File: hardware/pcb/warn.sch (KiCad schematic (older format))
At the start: 16 parts, among them CON2 MMCX_CONN, Q1 Q_NPN_BEC, U8 TPS61041, U9 ZXMHC6A07N8

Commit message: pre major restructuring commit
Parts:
- removed Q1: Q_NPN_BEC, Housings_SOT-23_SOT-143_TSOT-6:SOT-23, symbol Q_NPN_BEC-RESCUE-aero
- removed R15, R16: 3k, Resistors_SMD:R_0603, symbol R
- removed U9: ZXMHC6A07N8, Power_Integrations:SO-8, symbol ZXMHC6A07N8
- added Q1: BSS138, Housings_SOT-23_SOT-143_TSOT-6:SOT-23, symbol BSS138
- added R14: 30k, Resistors_SMD:R_0402, symbol R
- added U10, U11: BU4SU69G2, aero:SSOP-5, symbol BU4SU69G2
- added U12: NC7WZ17, Housings_SOT-23_SOT-143_TSOT-6:SC-70-6, symbol NC7WZ17
- C29: renamed from C32; footprint Capacitors_SMD:C_0603 -> Capacitors_SMD:C_0402
- C30: renamed from C33; footprint Capacitors_SMD:C_0603 -> Capacitors_SMD:C_0402
- C31: renamed from C34; footprint Capacitors_SMD:C_0603 -> Capacitors_SMD:C_0402
- L1: renamed from L4; footprint aero:SDR0703 -> aero:IND-744029100
- R11: renamed from R12; value 120 -> 200; footprint Resistors_SMD:R_0603 -> Resistors_SMD:R_0402
- R12: renamed from R13; footprint Resistors_SMD:R_0603 -> Resistors_SMD:R_0402
- R13: renamed from R14; value 140k -> 309k; footprint Resistors_SMD:R_0603 -> Resistors_SMD:R_0402
- renumbered D2 to D1, D3 to D2, U8 to U9
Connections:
- net labels added: +10V
- net labels removed: +24V
- wire segments 52 -> 38
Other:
- note removed: "Add a flyback diode?"
- note removed: "Confirm pin assignments of NPN"
- note removed: "NOTE: Update R when LED is picked out"
- note removed: "Using VBATT here is probably a bad idea"
- moved on the sheet: AUD1, C29, C30, C31, CON2, D2, L1, R12, R13, U9

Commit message: more progress on new layout
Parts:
- renumbered C29 to C27, C30 to C28, C31 to C29, R11 to R10, R12 to R11, R13 to R12, R14 to R13
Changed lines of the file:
@@
 $EndComp
 $Comp
-L C C29
+L C C27
 U 1 1 55381689
 P 1650 5475
-F 0 "C29" H 1675 5575 50  0000 L CNN
+F 0 "C27" H 1675 5575 50  0000 L CNN
 F 1 "4.7uF" H 1675 5375 50  0000 L CNN
 F 2 "Capacitors_SMD:C_0402" H 1688 5325 30  0001 C CNN
@@
 $EndComp
 $Comp
-L R R12
+L R R11
 U 1 1 55381851
 P 4200 5025
-F 0 "R12" V 4280 5025 50  0000 C CNN
+F 0 "R11" V 4280 5025 50  0000 C CNN
 F 1 "2.21m" V 4200 5025 50  0000 C CNN
 F 2 "Resistors_SMD:R_0402" V 4130 5025 30  0001 C CNN
@@
 $EndComp
 $Comp
-L R R13
+L R R12
 U 1 1 5538187A
 P 4200 5625
-F 0 "R13" V 4280 5625 50  0000 C CNN
+F 0 "R12" V 4280 5625 50  0000 C CNN
 F 1 "309k" V 4200 5625 50  0000 C CNN
 F 2 "Resistors_SMD:R_0402" V 4130 5625 30  0001 C CNN
@@
 $EndComp
 $Comp
-L C C30
+L C C28
 U 1 1 553818B9
 P 4600 5025
-F 0 "C30" H 4625 5125 50  0000 L CNN
+F 0 "C28" H 4625 5125 50  0000 L CNN
 F 1 "22pF" H 4625 4925 50  0000 L CNN
 F 2 "Capacitors_SMD:C_0402" H 4638 4875 30  0001 C CNN
@@
 $EndComp
 $Comp
-L C C31
+L C C29
 U 1 1 553818E7
 P 4950 5025
-F 0 "C31" H 4975 5125 50  0000 L CNN
+F 0 "C29" H 4975 5125 50  0000 L CNN
 F 1 "100nF" H 4975 4925 50  0000 L CNN
 F 2 "Capacitors_SMD:C_0402" H 4988 4875 30  0001 C CNN
@@
 $EndComp
 $Comp
-L R R11
+L R R10
 U 1 1 55381B8F
 P 2850 2800
-F 0 "R11" V 2930 2800 50  0000 C CNN
+F 0 "R10" V 2930 2800 50  0000 C CNN
 F 1 "200" V 2850 2800 50  0000 C CNN
 F 2 "Resistors_SMD:R_0402" V 2780 2800 30  0001 C CNN
@@
 $EndComp
 $Comp
-L R R14
+L R R13
 U 1 1 55B1064F
 P 6175 5000
-F 0 "R14" V 6255 5000 50  0000 C CNN
+F 0 "R13" V 6255 5000 50  0000 C CNN
 F 1 "30k" V 6175 5000 50  0000 C CNN
 F 2 "Resistors_SMD:R_0402" V 6105 5000 30  0001 C CNN

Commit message: pre-net import
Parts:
- added U14: NC7WZ17, Housings_SOT-23_SOT-143_TSOT-6:SC-70-6, symbol NC7WZ17
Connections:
- net +3V: now also U14.5 (+3V), U14.5 (+3V)
- net GND: now also U14.2 (GND), U14.2 (GND)
- net WARN_LED_A: now also U12.1
- net WARN_LED_B: now also U14.1, U14.3; no longer U12.1
- net at CON2.1 (SIG), U12.4: now also U12.6
- net at CON2.2 (GND), CON2.3 (GND), CON2.4 (GND)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: now also U14.4, U14.6; no longer U12.6
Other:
- moved on the sheet: U12A, U12B
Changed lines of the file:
@@
 Text HLabel 5675 5650 0    60   Input ~ 0
 PIEZO_OUT
-Text HLabel 7975 2575 0    60   Input ~ 0
+Text HLabel 7950 2575 0    60   Input ~ 0
 WARN_LED_A
-Text HLabel 7975 3100 0    60   Input ~ 0
+Text HLabel 7950 3500 0    60   Input ~ 0
 WARN_LED_B
 Text HLabel 1700 2800 0    60   Input ~ 0
@@
 EN needs to be at least\n1.2v
 $Comp
-L MMCX_CONN CON2
-U 1 1 5540F4C0
-P 9900 2675
-F 0 "CON2" H 10100 2875 60  0000 C CNN
-F 1 "MMCX_CONN" H 10050 2525 60  0000 C CNN
-F 2 "aero:CONMMCX002-SMD" H 9900 2675 60  0001 C CNN
-F 3 "" H 9900 2675 60  0000 C CNN
-	1    9900 2675
-	1    0    0    -1
-$EndComp
-$Comp
 L PIEZO AUD1
 U 1 1 554BE33E
@@
 L NC7WZ17 U12
 U 1 1 55B160CF
-P 8425 3100
-F 0 "U12" H 8525 3225 60  0000 C CNN
-F 1 "NC7WZ17" H 8600 2925 60  0001 C CNN
-F 2 "Housings_SOT-23_SOT-143_TSOT-6:SC-70-6" H 8425 3100 60  0001 C CNN
-F 3 "" H 8425 3100 60  0000 C CNN
-	1    8425 3100
+P 8475 2575
+F 0 "U12" H 8575 2700 60  0000 C CNN
+F 1 "NC7WZ17" H 8650 2400 60  0001 C CNN
+F 2 "Housings_SOT-23_SOT-143_TSOT-6:SC-70-6" H 8475 2575 60  0001 C CNN
+F 3 "" H 8475 2575 60  0000 C CNN
+	1    8475 2575
 	1    0    0    -1
 $EndComp
@@
 L NC7WZ17 U12
 U 2 1 55B161A1
-P 8450 2575
-F 0 "U12" H 8550 2700 60  0000 C CNN
-F 1 "NC7WZ17" H 8625 2400 60  0001 C CNN
-F 2 "Housings_SOT-23_SOT-143_TSOT-6:SC-70-6" H 8450 2575 60  0001 C CNN
-F 3 "" H 8450 2575 60  0000 C CNN
-	2    8450 2575
+P 8450 2925
+F 0 "U12" H 8550 3050 60  0000 C CNN
+F 1 "NC7WZ17" H 8625 2750 60  0001 C CNN
+F 2 "Housings_SOT-23_SOT-143_TSOT-6:SC-70-6" H 8450 2925 60  0001 C CNN
+F 3 "" H 8450 2925 60  0000 C CNN
+	2    8450 2925
 	1    0    0    -1
 $EndComp
@@
 Wire Wire Line
 	2350 2800 2700 2800
-Wire Wire Line
-	10675 2575 10675 3100
 Connection ~ 10675 2650
 Connection ~ 10675 2725
@@
 	5675 5650 5875 5650
 Wire Wire Line
-	8150 3100 7975 3100
-Wire Wire Line
-	7975 2575 8175 2575
-Wire Wire Line
-	8750 2575 9650 2575
-Wire Wire Line
-	10675 3100 8725 3100
-Wire Wire Line
 	3900 4725 6225 4725
+$Comp
+L NC7WZ17 U14
+U 1 1 561D6D8E
+P 8425 3500
+F 0 "U14" H 8525 3625 60  0000 C CNN
+F 1 "NC7WZ17" H 8600 3325 60  0001 C CNN
+F 2 "Housings_SOT-23_SOT-143_TSOT-6:SC-70-6" H 8425 3500 60  0001 C CNN
+F 3 "" H 8425 3500 60  0000 C CNN
+	1    8425 3500
+	1    0    0    -1
+$EndComp
+$Comp
+L NC7WZ17 U14
+U 2 1 561D6E0B
+P 8450 3925
+F 0 "U14" H 8550 4050 60  0000 C CNN
+F 1 "NC7WZ17" H 8625 3750 60  0001 C CNN
+F 2 "Housings_SOT-23_SOT-143_TSOT-6:SC-70-6" H 8450 3925 60  0001 C CNN
+F 3 "" H 8450 3925 60  0000 C CNN
+	2    8450 3925
+	1    0    0    -1
+$EndComp
+$Comp
+L MMCX_CONN CON2
+U 1 1 5540F4C0
+P 9900 2675
+F 0 "CON2" H 10100 2875 60  0000 C CNN
+F 1 "MMCX_CONN" H 10050 2525 60  0000 C CNN
+F 2 "aero:CONMMCX002-SMD" H 9900 2675 60  0001 C CNN
+F 3 "" H 9900 2675 60  0000 C CNN
+	1    9900 2675
+	1    0    0    -1
+$EndComp
+Wire Wire Line
+	7950 2575 8200 2575
+Wire Wire Line
+	8175 2925 8050 2925
+Wire Wire Line
+	8050 2925 8050 2575
+Connection ~ 8050 2575
+Wire Wire Line
+	8775 2575 9650 2575
+Wire Wire Line
+	8750 2925 9050 2925
+Wire Wire Line
+	9050 2925 9050 2575
+Connection ~ 9050 2575
+Wire Wire Line
+	7950 3500 8150 3500
+Wire Wire Line
+	8050 3500 8050 3925
+Wire Wire Line
+	8050 3925 8175 3925
+Connection ~ 8050 3500
+Wire Wire Line
+	10675 3500 8725 3500
+Wire Wire Line
+	10675 2575 10675 3500
+Wire Wire Line
+	8750 3925 9050 3925
+Wire Wire Line
+	9050 3925 9050 3500
+Connection ~ 9050 3500
 $EndSCHEMATC

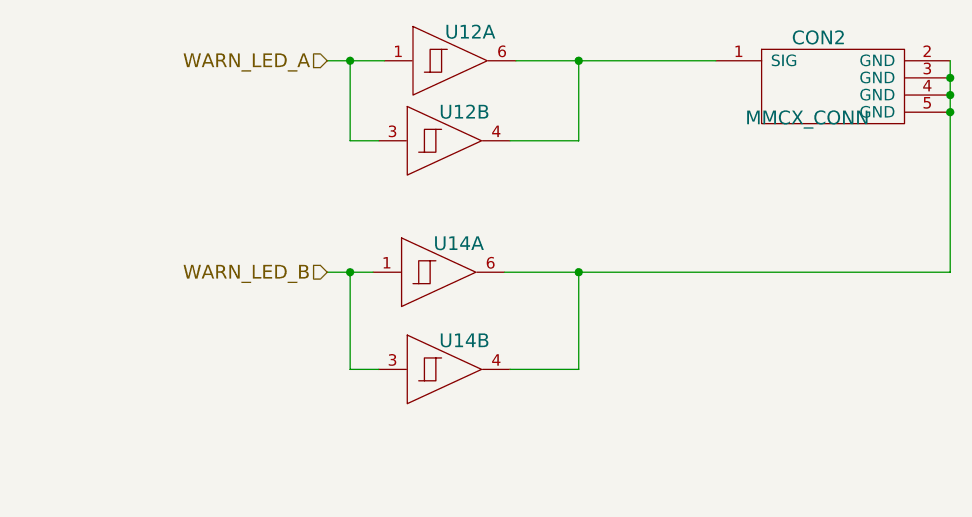
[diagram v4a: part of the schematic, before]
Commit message: passes DRC with stitching
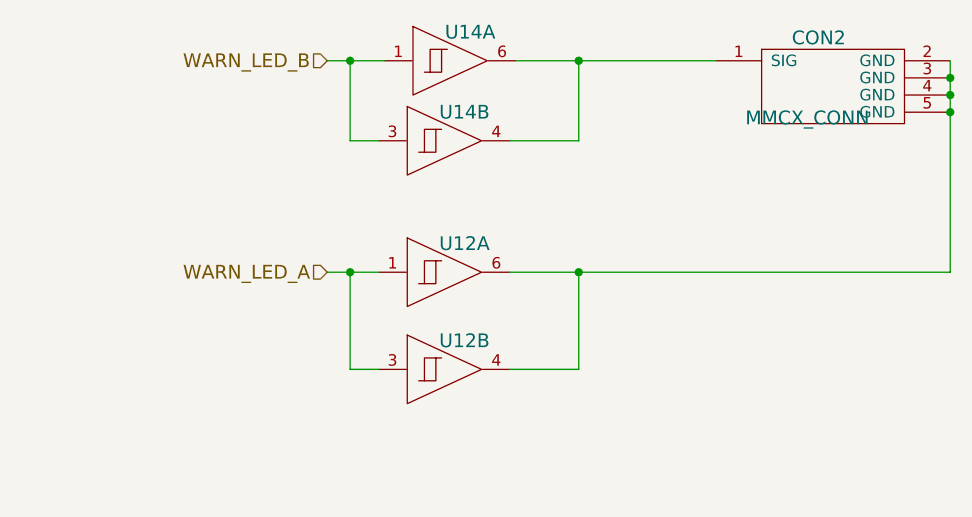
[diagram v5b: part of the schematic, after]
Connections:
- net at U12.4, U12.6: now also CON2.2 (GND), CON2.3 (GND), CON2.4 (GND), CON2.5 (GND); no longer CON2.1 (SIG)
- new net: CON2.1 (SIG), U14.4, U14.6
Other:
- moved on the sheet: U12A, U12B, U14A, U14B
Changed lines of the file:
@@
 Text HLabel 5675 5650 0    60   Input ~ 0
 PIEZO_OUT
+Text HLabel 7950 3500 0    60   Input ~ 0
+WARN_LED_A
 Text HLabel 7950 2575 0    60   Input ~ 0
-WARN_LED_A
-Text HLabel 7950 3500 0    60   Input ~ 0
 WARN_LED_B
 Text HLabel 1700 2800 0    60   Input ~ 0
@@
 L NC7WZ17 U12
 U 1 1 55B160CF
-P 8475 2575
-F 0 "U12" H 8575 2700 60  0000 C CNN
-F 1 "NC7WZ17" H 8650 2400 60  0001 C CNN
-F 2 "Housings_SOT-23_SOT-143_TSOT-6:SC-70-6" H 8475 2575 60  0001 C CNN
-F 3 "" H 8475 2575 60  0000 C CNN
-	1    8475 2575
+P 8450 3500
+F 0 "U12" H 8550 3625 60  0000 C CNN
+F 1 "NC7WZ17" H 8625 3325 60  0001 C CNN
+F 2 "Housings_SOT-23_SOT-143_TSOT-6:SC-70-6" H 8450 3500 60  0001 C CNN
+F 3 "" H 8450 3500 60  0000 C CNN
+	1    8450 3500
 	1    0    0    -1
 $EndComp
@@
 L NC7WZ17 U12
 U 2 1 55B161A1
-P 8450 2925
-F 0 "U12" H 8550 3050 60  0000 C CNN
-F 1 "NC7WZ17" H 8625 2750 60  0001 C CNN
-F 2 "Housings_SOT-23_SOT-143_TSOT-6:SC-70-6" H 8450 2925 60  0001 C CNN
-F 3 "" H 8450 2925 60  0000 C CNN
-	2    8450 2925
+P 8450 3925
+F 0 "U12" H 8550 4050 60  0000 C CNN
+F 1 "NC7WZ17" H 8625 3750 60  0001 C CNN
+F 2 "Housings_SOT-23_SOT-143_TSOT-6:SC-70-6" H 8450 3925 60  0001 C CNN
+F 3 "" H 8450 3925 60  0000 C CNN
+	2    8450 3925
 	1    0    0    -1
 $EndComp
@@
 	0    1    1    0
 $EndComp
-Wire Wire Line
-	2450 5475 2750 5475
-Wire Wire Line
-	1150 5075 1150 5275
-Wire Wire Line
-	1150 5275 2750 5275
-Wire Wire Line
-	1650 5325 1650 5275
-Connection ~ 1650 5275
-Wire Wire Line
-	1650 5625 1650 6025
-Wire Wire Line
-	2400 4725 2200 4725
-Wire Wire Line
-	2200 4725 2200 5275
-Connection ~ 2200 5275
-Wire Wire Line
-	3000 4725 3600 4725
-Wire Wire Line
-	3300 4975 3300 4725
-Connection ~ 3300 4725
-Wire Wire Line
-	4200 5175 4200 5475
-Wire Wire Line
-	3750 5375 4600 5375
-Connection ~ 4200 5375
-Wire Wire Line
-	1650 5975 6175 5975
-Wire Wire Line
-	3300 5975 3300 5825
-Connection ~ 1650 5975
-Wire Wire Line
-	4200 5975 4200 5775
-Connection ~ 3300 5975
-Wire Wire Line
-	4600 5375 4600 5175
-Wire Wire Line
-	4200 4725 4200 4875
-Wire Wire Line
-	4600 4725 4600 4875
-Connection ~ 4200 4725
-Wire Wire Line
-	4950 4725 4950 4875
-Connection ~ 4600 4725
-Wire Wire Line
-	4950 5175 4950 5975
-Connection ~ 4200 5975
-Connection ~ 4950 4725
-Wire Wire Line
-	3000 2800 3400 2800
-Wire Wire Line
-	3400 2800 3400 3000
-Wire Wire Line
-	1700 2800 1950 2800
-Wire Wire Line
-	2350 2800 2700 2800
-Connection ~ 10675 2650
-Connection ~ 10675 2725
-Connection ~ 10675 2800
-Wire Wire Line
-	7150 5325 7375 5325
-Wire Wire Line
-	7325 5800 7325 5325
-Connection ~ 7325 5325
-Wire Wire Line
-	7875 5325 7875 5800
-Wire Wire Line
-	7875 5800 7425 5800
-Wire Wire Line
-	6175 5325 6650 5325
-Wire Wire Line
-	6175 5150 6175 5400
-Connection ~ 6175 5325
-Wire Wire Line
-	6175 4575 6175 4850
-Connection ~ 6175 4725
-Wire Wire Line
-	6175 5975 6175 5800
-Connection ~ 4950 5975
-Wire Wire Line
-	5675 5650 5875 5650
-Wire Wire Line
-	3900 4725 6225 4725
 $Comp
 L NC7WZ17 U14
 U 1 1 561D6D8E
-P 8425 3500
-F 0 "U14" H 8525 3625 60  0000 C CNN
-F 1 "NC7WZ17" H 8600 3325 60  0001 C CNN
-F 2 "Housings_SOT-23_SOT-143_TSOT-6:SC-70-6" H 8425 3500 60  0001 C CNN
-F 3 "" H 8425 3500 60  0000 C CNN
-	1    8425 3500
+P 8475 2575
+F 0 "U14" H 8575 2700 60  0000 C CNN
+F 1 "NC7WZ17" H 8650 2400 60  0001 C CNN
+F 2 "Housings_SOT-23_SOT-143_TSOT-6:SC-70-6" H 8475 2575 60  0001 C CNN
+F 3 "" H 8475 2575 60  0000 C CNN
+	1    8475 2575
 	1    0    0    -1
 $EndComp
@@
 L NC7WZ17 U14
 U 2 1 561D6E0B
-P 8450 3925
-F 0 "U14" H 8550 4050 60  0000 C CNN
-F 1 "NC7WZ17" H 8625 3750 60  0001 C CNN
-F 2 "Housings_SOT-23_SOT-143_TSOT-6:SC-70-6" H 8450 3925 60  0001 C CNN
-F 3 "" H 8450 3925 60  0000 C CNN
-	2    8450 3925
+P 8450 2925
+F 0 "U14" H 8550 3050 60  0000 C CNN
+F 1 "NC7WZ17" H 8625 2750 60  0001 C CNN
+F 2 "Housings_SOT-23_SOT-143_TSOT-6:SC-70-6" H 8450 2925 60  0001 C CNN
+F 3 "" H 8450 2925 60  0000 C CNN
+	2    8450 2925
 	1    0    0    -1
 $EndComp
@@
 $EndComp
 Wire Wire Line
+	2450 5475 2750 5475
+Wire Wire Line
+	1150 5075 1150 5275
+Wire Wire Line
+	1150 5275 2750 5275
+Wire Wire Line
+	1650 5325 1650 5275
+Connection ~ 1650 5275
+Wire Wire Line
+	1650 5625 1650 6025
+Wire Wire Line
+	2400 4725 2200 4725
+Wire Wire Line
+	2200 4725 2200 5275
+Connection ~ 2200 5275
+Wire Wire Line
+	3000 4725 3600 4725
+Wire Wire Line
+	3300 4975 3300 4725
+Connection ~ 3300 4725
+Wire Wire Line
+	4200 5175 4200 5475
+Wire Wire Line
+	3750 5375 4600 5375
+Connection ~ 4200 5375
+Wire Wire Line
+	1650 5975 6175 5975
+Wire Wire Line
+	3300 5975 3300 5825
+Connection ~ 1650 5975
+Wire Wire Line
+	4200 5975 4200 5775
+Connection ~ 3300 5975
+Wire Wire Line
+	4600 5375 4600 5175
+Wire Wire Line
+	4200 4725 4200 4875
+Wire Wire Line
+	4600 4725 4600 4875
+Connection ~ 4200 4725
+Wire Wire Line
+	4950 4725 4950 4875
+Connection ~ 4600 4725
+Wire Wire Line
+	4950 5175 4950 5975
+Connection ~ 4200 5975
+Connection ~ 4950 4725
+Wire Wire Line
+	3000 2800 3400 2800
+Wire Wire Line
+	3400 2800 3400 3000
+Wire Wire Line
+	1700 2800 1950 2800
+Wire Wire Line
+	2350 2800 2700 2800
+Connection ~ 10675 2650
+Connection ~ 10675 2725
+Connection ~ 10675 2800
+Wire Wire Line
+	7150 5325 7375 5325
+Wire Wire Line
+	7325 5800 7325 5325
+Connection ~ 7325 5325
+Wire Wire Line
+	7875 5325 7875 5800
+Wire Wire Line
+	7875 5800 7425 5800
+Wire Wire Line
+	6175 5325 6650 5325
+Wire Wire Line
+	6175 5150 6175 5400
+Connection ~ 6175 5325
+Wire Wire Line
+	6175 4575 6175 4850
+Connection ~ 6175 4725
+Wire Wire Line
+	6175 5975 6175 5800
+Connection ~ 4950 5975
+Wire Wire Line
+	5675 5650 5875 5650
+Wire Wire Line
+	3900 4725 6225 4725
+Wire Wire Line
 	7950 2575 8200 2575
-Wire Wire Line
-	8175 2925 8050 2925
 Wire Wire Line
 	8050 2925 8050 2575
@@
 Connection ~ 9050 2575
 Wire Wire Line
-	7950 3500 8150 3500
+	7950 3500 8175 3500
 Wire Wire Line
 	8050 3500 8050 3925
@@
 Connection ~ 8050 3500
 Wire Wire Line
-	10675 3500 8725 3500
-Wire Wire Line
-	10675 2575 10675 3500
+	10675 3500 10675 2575
 Wire Wire Line
 	8750 3925 9050 3925
@@
 	9050 3925 9050 3500
 Connection ~ 9050 3500
+Wire Wire Line
+	8750 3500 10675 3500
+Wire Wire Line
+	8175 2925 8050 2925
 $EndSCHEMATC
